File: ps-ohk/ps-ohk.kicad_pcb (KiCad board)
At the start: 2 copper layers, 26 parts

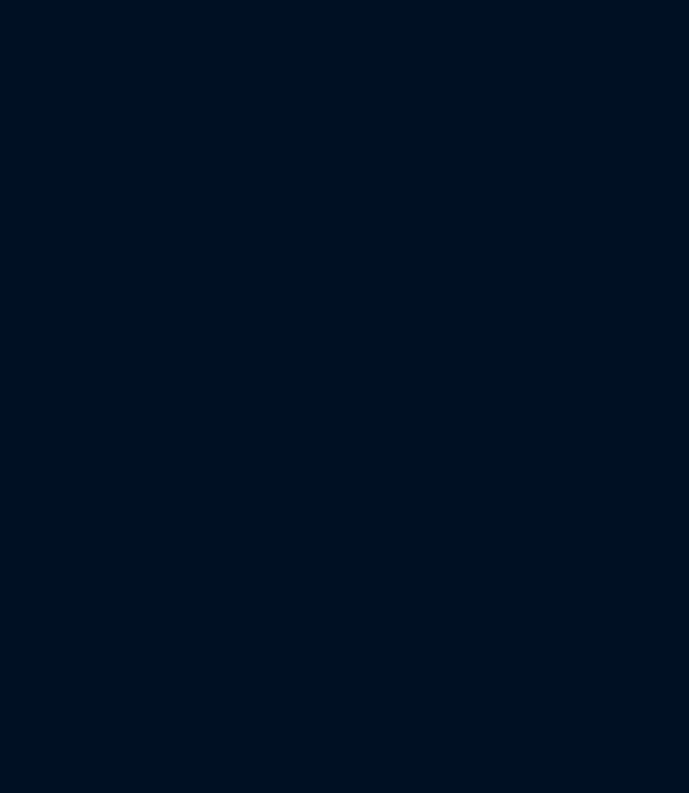
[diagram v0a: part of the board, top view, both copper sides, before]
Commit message: Added 40-pin IO Expander to project
Will make use of two of them

Signed-off-by: Dylan Turner <dylan.turner@tutanota.com>
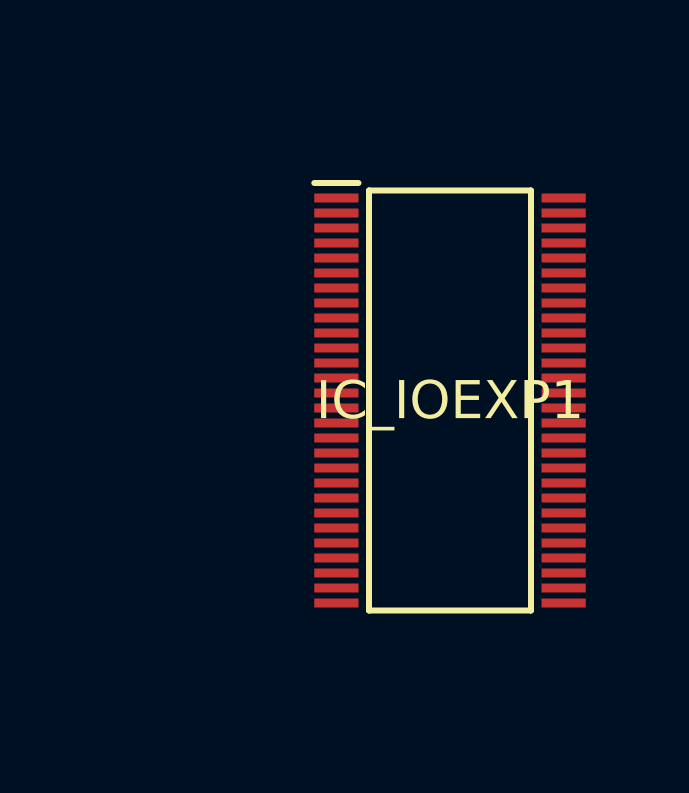
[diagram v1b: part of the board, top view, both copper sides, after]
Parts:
- added IC_IOEXP1: PCA9505DGGY, PCA9505DGGY:SOP50P810X120-56N, F.Cu at (165.2, 81.8)
